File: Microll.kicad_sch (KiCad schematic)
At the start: 0 parts

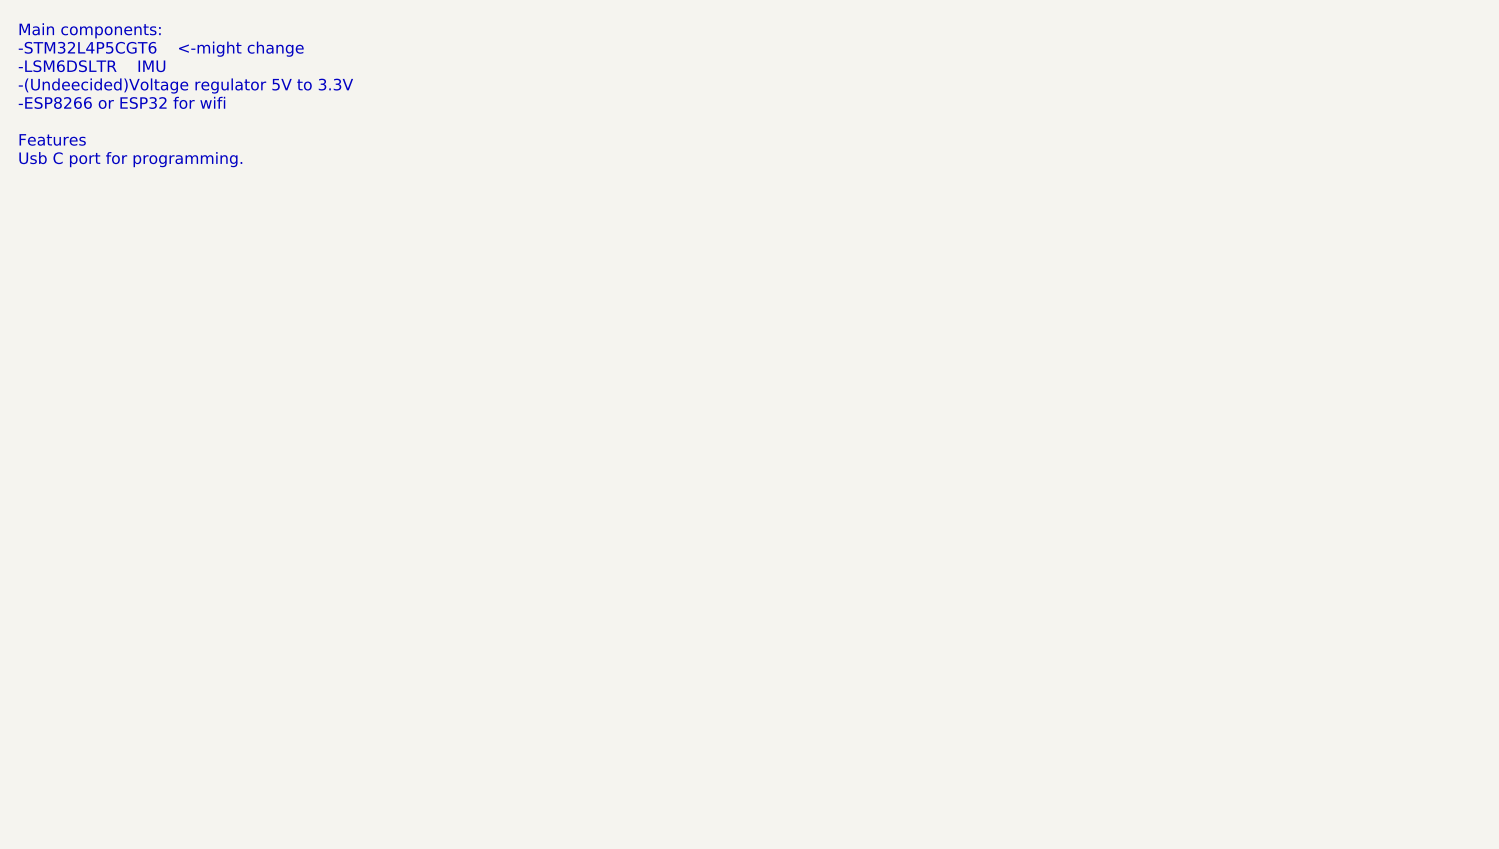
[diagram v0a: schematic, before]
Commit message: More motes on the board main components.
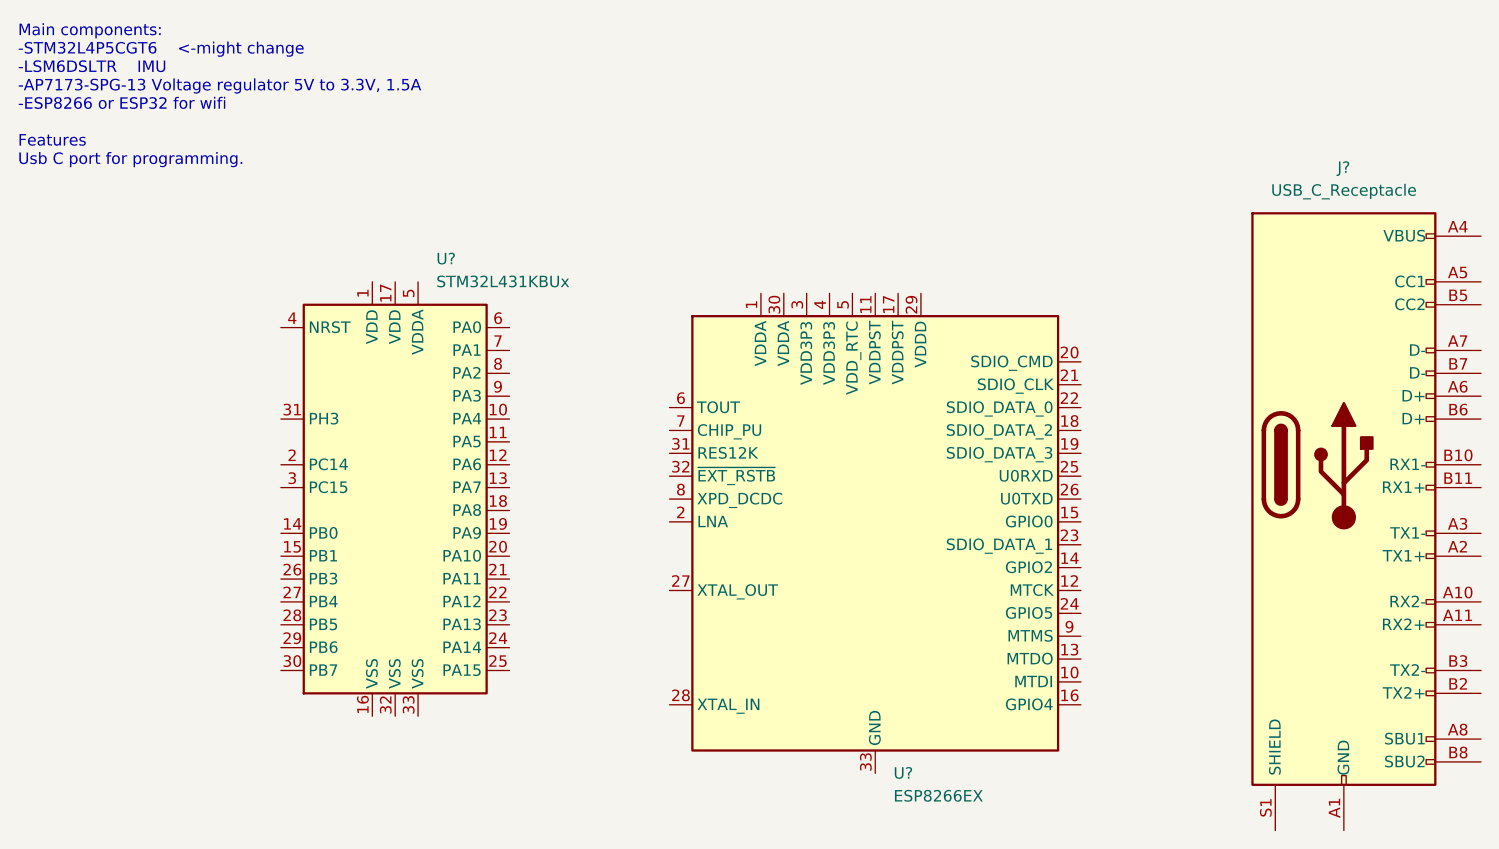
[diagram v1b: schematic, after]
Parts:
- added J?: USB_C_Receptacle, symbol Connector:USB_C_Receptacle
- added U?: STM32L431KBUx, Package_DFN_QFN:QFN-32-1EP_5x5mm_P0.5mm_EP3.45x3.45mm, symbol MCU_ST_STM32L4:STM32L431KBUx
- added U?: ESP8266EX, Package_DFN_QFN:QFN-32-1EP_5x5mm_P0.5mm_EP3.45x3.45mm, symbol MCU_Espressif:ESP8266EX
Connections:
- new net: J?.A1 (GND), J?.A12 (GND), J?.B1 (GND), J?.B12 (GND)
- new net: J?.A4 (VBUS), J?.A9 (VBUS), J?.B4 (VBUS), J?.B9 (VBUS)
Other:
- note added: "Main components: -STM32L4P5CGT6 <-might change -LSM6DSLTR IMU -AP7173-SPG-13 Voltage regulator 5V to 3.3V, 1.5A -ESP8266 or ESP32 for wifi Features Usb C port for programming."
- note removed: "Main components: -STM32L4P5CGT6 <-might change -LSM6DSLTR IMU -(Undeecided)Voltage regulator 5V to 3.3V -ESP8266 or ESP32 for wifi Features Usb C port for programming."
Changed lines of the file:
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@@
 (kicad_sch (version 20211123) (generator eeschema)
   (paper "A4")
-  (text "Main components:\n-STM32L4P5CGT6	<-might change	\n-LSM6DSLTR	IMU\n-(Undeecided)Voltage regulator 5V to 3.3V\n-ESP8266 or ESP32 for wifi\n\nFeatures\nUsb C port for programming."
+  (text "Main components:\n-STM32L4P5CGT6	<-might change	\n-LSM6DSLTR	IMU\n-AP7173-SPG-13 Voltage regulator 5V to 3.3V, 1.5A\n-ESP8266 or ESP32 for wifi\n\nFeatures\nUsb C port for programming."
     (at 59.69 50.8 0)
     (effects (font (size 1.27 1.27)) (justify left bottom))
+  )
+  (symbol (lib_id "MCU_ST_STM32L4:STM32L431KBUx") (at 101.6 86.36 0) (unit 1)
+    (in_bom yes) (on_board yes) (fields_autoplaced)
+    (property "Reference" "U?" (id 0) (at 106.1594 60.96 0)
+      (effects (font (size 1.27 1.27)) (justify left))
+    )
+    (property "Value" "STM32L431KBUx" (id 1) (at 106.1594 63.5 0)
+      (effects (font (size 1.27 1.27)) (justify left))
+    )
+    (property "Footprint" "Package_DFN_QFN:QFN-32-1EP_5x5mm_P0.5mm_EP3.45x3.45mm" (id 2) (at 91.44 109.22 0)
+      (effects (font (size 1.27 1.27)) (justify right) hide)
+    )
+    (property "Datasheet" "http://www.st.com/st-web-ui/static/active/en/resource/technical/document/datasheet/DM00257211.pdf" (id 3) (at 101.6 86.36 0)
+      (effects (font (size 1.27 1.27)) hide)
+    )
+    (pin "1")
+    (pin "10")
+    (pin "11")
+    (pin "12")
+    (pin "13")
+    (pin "14")
+    (pin "15")
+    (pin "16")
+    (pin "17")
+    (pin "18")
+    (pin "19")
+    (pin "2")
+    (pin "20")
+    (pin "21")
+    (pin "22")
+    (pin "23")
+    (pin "24")
+    (pin "25")
+    (pin "26")
+    (pin "27")
+    (pin "28")
+    (pin "29")
+    (pin "3")
+    (pin "30")
+    (pin "31")
+    (pin "32")
+    (pin "33")
+    (pin "4")
+    (pin "5")
+    (pin "6")
+    (pin "7")
+    (pin "8")
+    (pin "9")
+  )
+  (symbol (lib_id "MCU_Espressif:ESP8266EX") (at 154.94 90.17 0) (unit 1)
+    (in_bom yes) (on_board yes) (fields_autoplaced)
+    (property "Reference" "U?" (id 0) (at 156.9594 118.11 0)
+      (effects (font (size 1.27 1.27)) (justify left))
+    )
+    (property "Value" "ESP8266EX" (id 1) (at 156.9594 120.65 0)
+      (effects (font (size 1.27 1.27)) (justify left))
+    )
+    (property "Footprint" "Package_DFN_QFN:QFN-32-1EP_5x5mm_P0.5mm_EP3.45x3.45mm" (id 2) (at 154.94 123.19 0)
+      (effects (font (size 1.27 1.27)) hide)
+    )
+    (property "Datasheet" "http://espressif.com/sites/default/files/documentation/0a-esp8266ex_datasheet_en.pdf" (id 3) (at 157.48 123.19 0)
+      (effects (font (size 1.27 1.27)) hide)
+    )
+    (pin "1")
+    (pin "10")
+    (pin "11")
+    (pin "12")
+    (pin "13")
+    (pin "14")
+    (pin "15")
+    (pin "16")
+    (pin "17")
+    (pin "18")
+    (pin "19")
+    (pin "2")
+    (pin "20")
+    (pin "21")
+    (pin "22")
+    (pin "23")
+    (pin "24")
+    (pin "25")
+    (pin "26")
+    (pin "27")
+    (pin "28")
+    (pin "29")
+    (pin "3")
+    (pin "30")
+    (pin "31")
+    (pin "32")
+    (pin "33")
+    (pin "4")
+    (pin "5")
+    (pin "6")
+    (pin "7")
+    (pin "8")
+    (pin "9")
+  )
+  (symbol (lib_id "Connector:USB_C_Receptacle") (at 207.01 83.82 0) (unit 1)
+    (in_bom yes) (on_board yes) (fields_autoplaced)
+    (property "Reference" "J?" (id 0) (at 207.01 50.8 0))
+    (property "Value" "USB_C_Receptacle" (id 1) (at 207.01 53.34 0))
+    (property "Footprint" "" (id 2) (at 210.82 83.82 0)
+      (effects (font (size 1.27 1.27)) hide)
+    )
+    (property "Datasheet" "https://www.usb.org/sites/default/files/documents/usb_type-c.zip" (id 3) (at 210.82 83.82 0)
+      (effects (font (size 1.27 1.27)) hide)
+    )
+    (pin "A1")
+    (pin "A10")
+    (pin "A11")
+    (pin "A12")
+    (pin "A2")
+    (pin "A3")
+    (pin "A4")
+    (pin "A5")
+    (pin "A6")
+    (pin "A7")
+    (pin "A8")
+    (pin "A9")
+    (pin "B1")
+    (pin "B10")
+    (pin "B11")
+    (pin "B12")
+    (pin "B2")
+    (pin "B3")
+    (pin "B4")
+    (pin "B5")
+    (pin "B6")
+    (pin "B7")
+    (pin "B8")
+    (pin "B9")
+    (pin "S1")
   )
   (sheet_instances
     (path "/" (page "1"))
   )
+  (symbol_instances
+    (path "/9dc9595c-915c-4807-bd39-25a9004629d5"
+      (reference "J?") (unit 1) (value "USB_C_Receptacle") (footprint "")
+    )
+    (path "/086be992-52ad-4b7c-be4a-eeec54e5d292"
+      (reference "U?") (unit 1) (value "STM32L431KBUx") (footprint "Package_DFN_QFN:QFN-32-1EP_5x5mm_P0.5mm_EP3.45x3.45mm")
+    )
+    (path "/6eda52df-143b-46e2-ab78-c0c82ad2ea2c"
+      (reference "U?") (unit 1) (value "ESP8266EX") (footprint "Package_DFN_QFN:QFN-32-1EP_5x5mm_P0.5mm_EP3.45x3.45mm")
+    )
+  )
 )

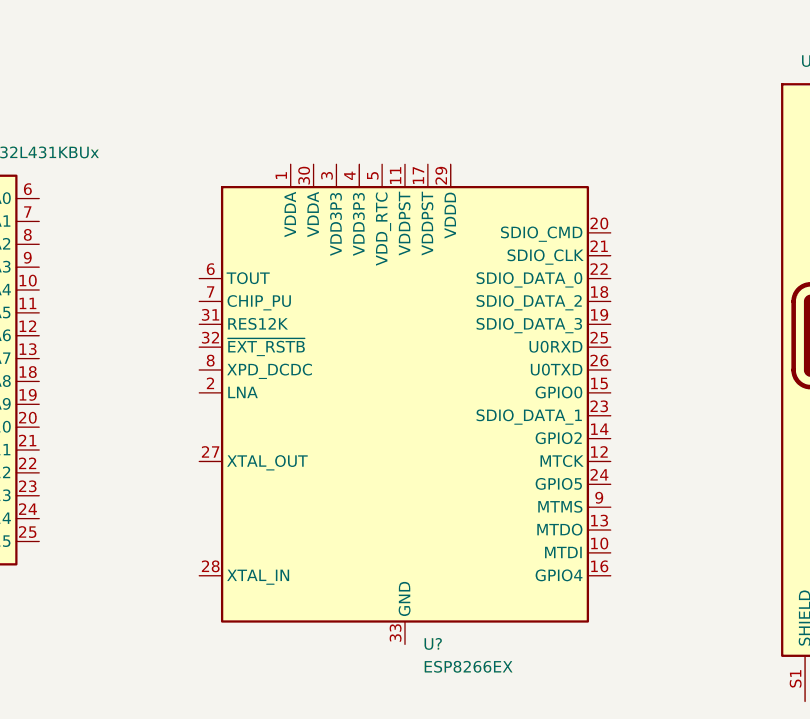
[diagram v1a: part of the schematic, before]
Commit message: Finished footprint for ESP32
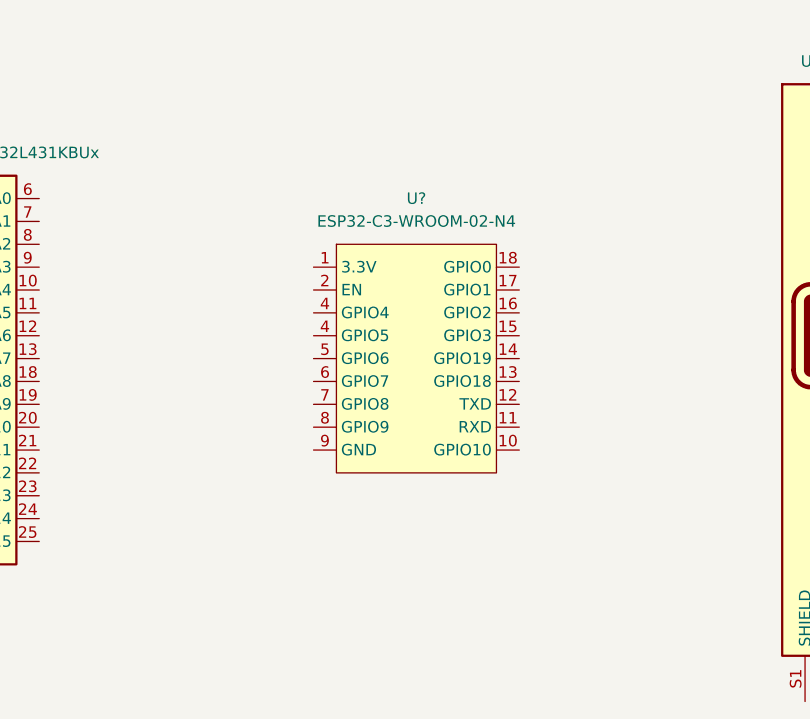
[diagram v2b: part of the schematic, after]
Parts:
- removed U?: ESP8266EX, Package_DFN_QFN:QFN-32-1EP_5x5mm_P0.5mm_EP3.45x3.45mm, symbol MCU_Espressif:ESP8266EX
- added U?: ESP32-C3-WROOM-02-N4, ESP32:ESP32-C3-WROOM-02-N4, symbol ESP32:ESP32-C3-WROOM-02-N4
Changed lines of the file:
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@@
     (pin "9")
   )
-  (symbol (lib_id "MCU_Espressif:ESP8266EX") (at 154.94 90.17 0) (unit 1)
+  (symbol (lib_id "ESP32:ESP32-C3-WROOM-02-N4") (at 156.21 82.55 0) (unit 1)
     (in_bom yes) (on_board yes) (fields_autoplaced)
-    (property "Reference" "U?" (id 0) (at 156.9594 118.11 0)
-      (effects (font (size 1.27 1.27)) (justify left))
-    )
-    (property "Value" "ESP8266EX" (id 1) (at 156.9594 120.65 0)
-      (effects (font (size 1.27 1.27)) (justify left))
-    )
-    (property "Footprint" "Package_DFN_QFN:QFN-32-1EP_5x5mm_P0.5mm_EP3.45x3.45mm" (id 2) (at 154.94 123.19 0)
+    (property "Reference" "U?" (id 0) (at 156.21 68.58 0))
+    (property "Value" "ESP32-C3-WROOM-02-N4" (id 1) (at 156.21 71.12 0))
+    (property "Footprint" "ESP32:ESP32-C3-WROOM-02-N4" (id 2) (at 156.21 82.55 0)
       (effects (font (size 1.27 1.27)) hide)
     )
-    (property "Datasheet" "http://espressif.com/sites/default/files/documentation/0a-esp8266ex_datasheet_en.pdf" (id 3) (at 157.48 123.19 0)
+    (property "Datasheet" "" (id 3) (at 156.21 82.55 0)
       (effects (font (size 1.27 1.27)) hide)
     )
@@
     (pin "17")
     (pin "18")
-    (pin "19")
     (pin "2")
-    (pin "20")
-    (pin "21")
-    (pin "22")
-    (pin "23")
-    (pin "24")
-    (pin "25")
-    (pin "26")
-    (pin "27")
-    (pin "28")
-    (pin "29")
-    (pin "3")
-    (pin "30")
-    (pin "31")
-    (pin "32")
-    (pin "33")
+    (pin "4")
     (pin "4")
     (pin "5")
@@
       (reference "U?") (unit 1) (value "STM32L431KBUx") (footprint "Package_DFN_QFN:QFN-32-1EP_5x5mm_P0.5mm_EP3.45x3.45mm")
     )
-    (path "/6eda52df-143b-46e2-ab78-c0c82ad2ea2c"
-      (reference "U?") (unit 1) (value "ESP8266EX") (footprint "Package_DFN_QFN:QFN-32-1EP_5x5mm_P0.5mm_EP3.45x3.45mm")
+    (path "/3757d3b5-a25c-4772-93e2-fe7135fc4c50"
+      (reference "U?") (unit 1) (value "ESP32-C3-WROOM-02-N4") (footprint "ESP32:ESP32-C3-WROOM-02-N4")
     )
   )
